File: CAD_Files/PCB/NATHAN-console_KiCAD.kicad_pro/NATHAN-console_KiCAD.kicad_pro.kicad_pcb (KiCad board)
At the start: 2 copper layers, 93 x 84 mm, 38 parts

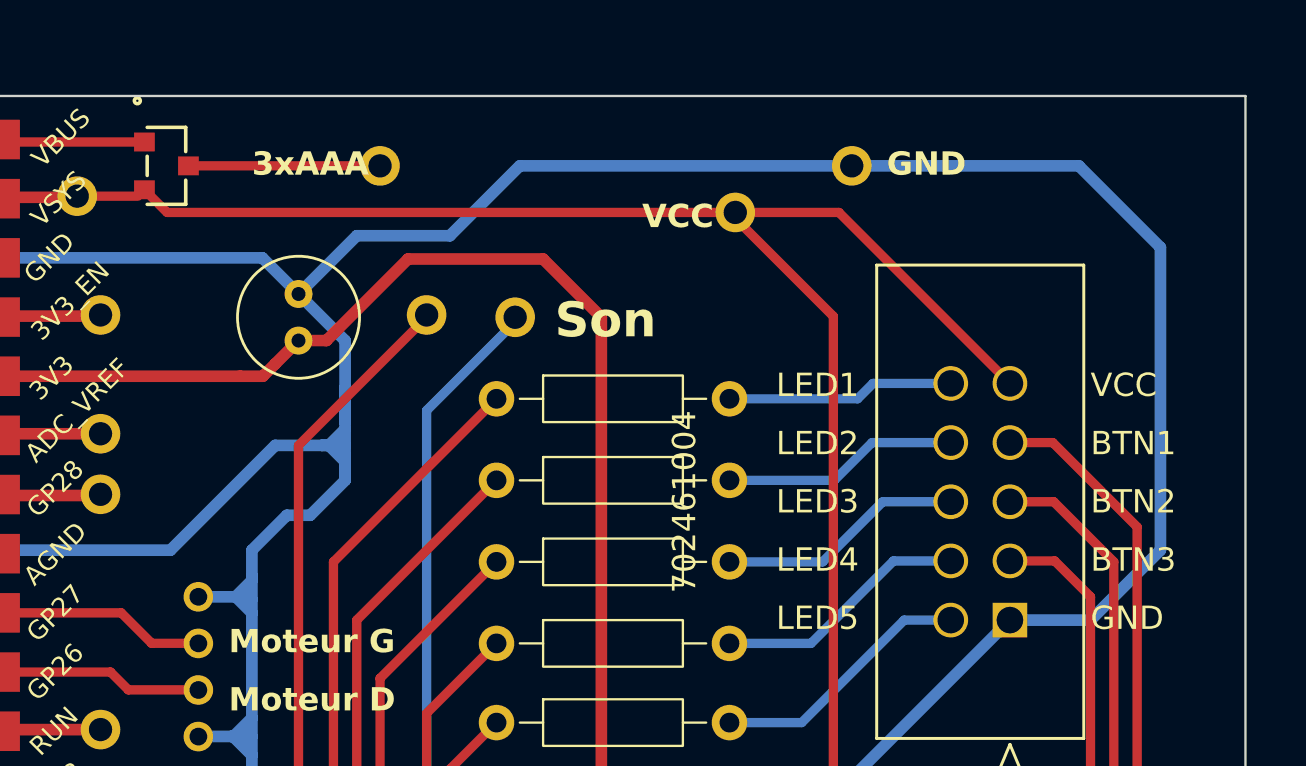
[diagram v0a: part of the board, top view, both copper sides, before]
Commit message: Add footprint information for Reverb modules and create autosave lock file
- Added fp-info-cache for two Reverb modules (BTDR-1H and BTDR-1V) with relevant details and links.
- Created an autosave lock file for the KiCAD project to prevent concurrent edits.
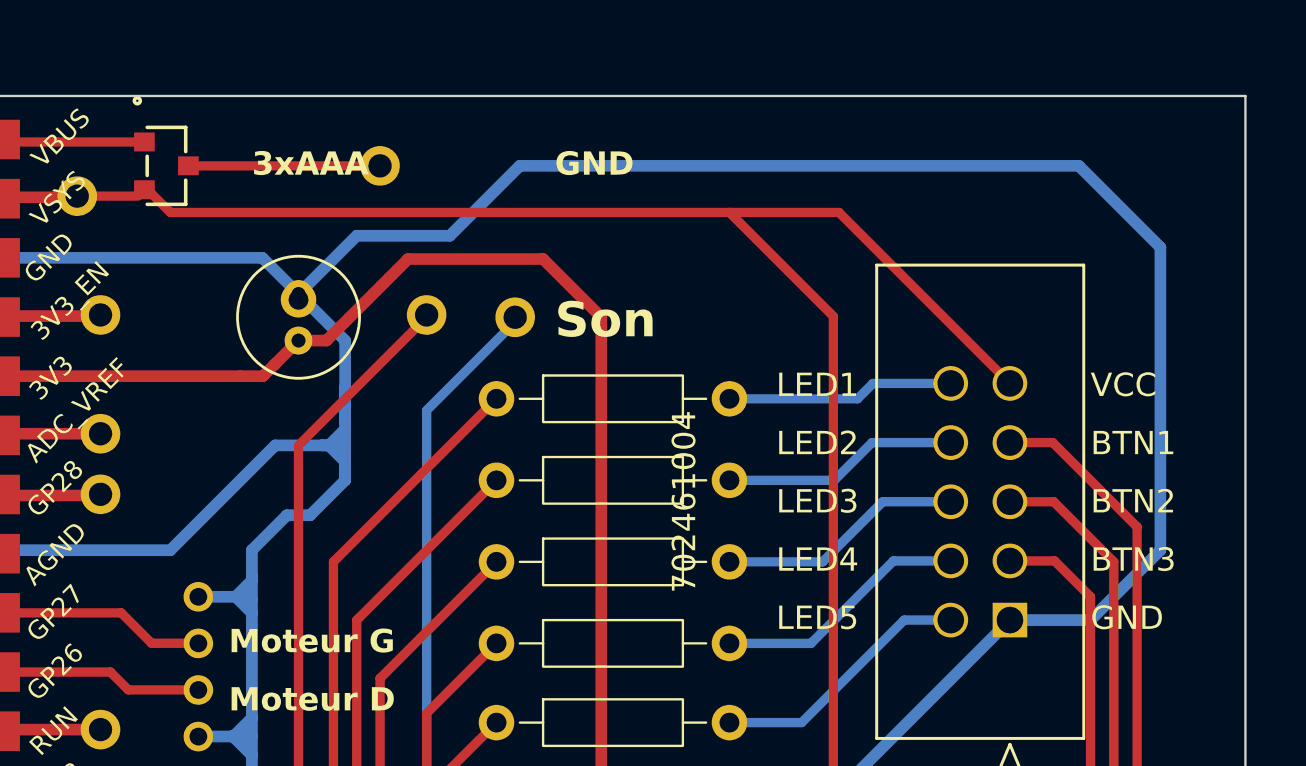
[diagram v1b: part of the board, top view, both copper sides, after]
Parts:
- removed the ? at (374.2, 154.0)
- removed the ? at (379.2, 152.0)
- added ?: , , F.Cu at (374.0, 154.0)
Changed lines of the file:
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@@
 	(footprint ""
 		(layer "F.Cu")
-		(at 309 170)
+		(at 374 154)
 		(property "Reference" ""
 			(at 0 0 0)
@@
 		)
 		(pad "1" thru_hole circle
-			(at 0 0)
-			(size 1.7 1.7)
-			(drill 1)
+			(at -18.5 3.75)
+			(size 1.524 1.524)
+			(drill 0.85)
 			(layers "*.Cu" "*.Mask")
 			(remove_unused_layers no)
+			(net 3 "VCC")
 		)
 	)
 	(footprint ""
 		(layer "F.Cu")
-		(at 315 189)
+		(at 309 170)
 		(property "Reference" ""
 			(at 0 0 0)
@@
 	(footprint ""
 		(layer "F.Cu")
-		(at 379.25 152)
+		(at 315 189)
 		(property "Reference" ""
 			(at 0 0 0)
@@
 			(layers "*.Cu" "*.Mask")
 			(remove_unused_layers no)
-			(net 1 "GND")
 		)
 	)
@@
 	(footprint ""
 		(layer "F.Cu")
-		(at 374.25 154)
-		(property "Reference" ""
-			(at 0 0 0)
-			(unlocked yes)
-			(layer "F.SilkS")
-			(effects
-				(font
-					(size 1.27 1.27)
-				)
-			)
-		)
-		(property "Value" ""
-			(at 0 0 0)
-			(unlocked yes)
-			(layer "F.Fab")
-			(effects
-				(font
-					(size 1.27 1.27)
-				)
-			)
-		)
-		(property "Footprint" ""
-			(at 0 0 0)
-			(unlocked yes)
-			(layer "F.Fab")
-			(hide yes)
-			(effects
-				(font
-					(size 1.27 1.27)
-				)
-			)
-		)
-		(property "Datasheet" ""
-			(at 0 0 0)
-			(unlocked yes)
-			(layer "F.Fab")
-			(hide yes)
-			(effects
-				(font
-					(size 1.27 1.27)
-				)
-			)
-		)
-		(property "Description" ""
-			(at 0 0 0)
-			(unlocked yes)
-			(layer "F.Fab")
-			(hide yes)
-			(effects
-				(font
-					(size 1.27 1.27)
-				)
-			)
-		)
-		(pad "1" thru_hole circle
-			(at 0 0)
-			(size 1.7 1.7)
-			(drill 1)
-			(layers "*.Cu" "*.Mask")
-			(remove_unused_layers no)
-			(net 3 "VCC")
-		)
-	)
-	(footprint ""
-		(layer "F.Cu")
 		(at 359 152)
 		(property "Reference" ""
@@
 		)
 	)
-	(gr_text "VCC"
-		(at 370.25 154.75 0)
-		(layer "F.SilkS")
-		(effects
-			(font
-				(size 1 1)
-				(thickness 0.2)
-				(bold yes)
-			)
-			(justify left bottom)
-		)
-	)
 	(gr_text "Son"
 		(at 366.5 159.5 0)
@@
 	)
 	(gr_text "GND"
-		(at 380.75 152.5 0)
+		(at 366.5 152.5 0)
 		(layer "F.SilkS")
 		(effects
@@
 	)
 	(segment
-		(start 358 155)
-		(end 355.5 157.5)
-		(width 0.5)
-		(layer "B.Cu")
-		(net 1)
-	)
-	(segment
 		(start 352.795101 170.5)
 		(end 352.8 170.495101)
@@
 	)
 	(segment
-		(start 386.04 171.5)
-		(end 389.5 171.5)
-		(width 0.5)
-		(layer "B.Cu")
-		(net 1)
-	)
-	(segment
 		(start 353.5 180.7)
 		(end 353.5 180.6)
@@
 	)
 	(segment
-		(start 379.25 152)
-		(end 365 152)
+		(start 354.5 164)
+		(end 356.5 164)
 		(width 0.5)
 		(layer "B.Cu")
@@
 	)
 	(segment
-		(start 354.5 164)
-		(end 356.5 164)
+		(start 311 180.5)
+		(end 311 180.9)
 		(width 0.5)
 		(layer "B.Cu")
@@
 	)
 	(segment
-		(start 311 180.5)
-		(end 311 180.9)
+		(start 365 152)
+		(end 389 152)
 		(width 0.5)
 		(layer "B.Cu")
@@
 	)
 	(segment
-		(start 365 152)
-		(end 362 155)
-		(width 0.5)
-		(layer "B.Cu")
-		(net 1)
-	)
-	(segment
 		(start 311 181.8)
 		(end 311 181.75)
@@
 	)
 	(segment
+		(start 362 155)
+		(end 358 155)
+		(width 0.5)
+		(layer "B.Cu")
+		(net 1)
+	)
+	(segment
 		(start 352.6 176.495099)
 		(end 353.495099 176.495099)
@@
 	)
 	(segment
-		(start 389 152)
-		(end 379.25 152)
+		(start 357.5 163)
+		(end 357.5 163.3)
 		(width 0.5)
 		(layer "B.Cu")
@@
 	)
 	(segment
-		(start 357.5 163)
-		(end 357.5 163.3)
+		(start 392.5 168.5)
+		(end 389.5 171.5)
 		(width 0.5)
 		(layer "B.Cu")
@@
 	)
 	(segment
+		(start 365 152)
+		(end 362 155)
+		(width 0.5)
+		(layer "B.Cu")
+		(net 1)
+	)
+	(segment
 		(start 313.35 168.65)
 		(end 311.85 168.65)
@@
 	)
 	(segment
+		(start 389.5 171.5)
+		(end 386.04 171.5)
+		(width 0.5)
+		(layer "B.Cu")
+		(net 1)
+	)
+	(segment
 		(start 323.11 181.35)
 		(end 312.1 181.35)
@@
 	)
 	(segment
-		(start 389.5 171.5)
-		(end 392.5 168.5)
-		(width 0.5)
-		(layer "B.Cu")
-		(net 1)
-	)
-	(segment
 		(start 353.95 155.95)
 		(end 355.5 157.5)
@@
 	)
 	(segment
-		(start 392.5 168.5)
+		(start 389 152)
 		(end 392.5 155.5)
 		(width 0.5)
@@
 	)
 	(segment
-		(start 311 176.9)
-		(end 311 180.5)
+		(start 358 155)
+		(end 355.5 157.5)
 		(width 0.5)
 		(layer "B.Cu")
@@
 	)
 	(segment
-		(start 311 175.2)
-		(end 311 175.1)
+		(start 311 176.9)
+		(end 311 180.5)
 		(width 0.5)
 		(layer "B.Cu")
@@
 	)
 	(segment
-		(start 392.5 155.5)
-		(end 389 152)
+		(start 311 175.2)
+		(end 311 175.1)
 		(width 0.5)
 		(layer "B.Cu")
@@
 	)
 	(segment
+		(start 392.5 155.5)
+		(end 392.5 168.5)
+		(width 0.5)
+		(layer "B.Cu")
+		(net 1)
+	)
+	(segment
 		(start 309.5 224)
 		(end 312 226.5)
@@
 	)
 	(segment
-		(start 362 155)
-		(end 358 155)
-		(width 0.5)
-		(layer "B.Cu")
-		(net 1)
-	)
-	(segment
 		(start 312 226.5)
 		(end 316.5 226.5)
@@
 	)
 	(segment
-		(start 378.46 158.46)
-		(end 374.25 154.25)
+		(start 348.885001 153.024999)
+		(end 349.024999 153.024999)
 		(width 0.4)
 		(layer "F.Cu")
@@
 	)
 	(segment
-		(start 386.04 161.34)
-		(end 378.7 154)
-		(width 0.4)
+		(start 340.95 153.35)
+		(end 345.95 153.35)
+		(width 0.5)
 		(layer "F.Cu")
 		(net 3)
 	)
 	(segment
-		(start 340.95 153.35)
-		(end 345.95 153.35)
-		(width 0.5)
+		(start 378.7 154)
+		(end 386.04 161.34)
+		(width 0.4)
 		(layer "F.Cu")
 		(net 3)
@@
 	)
 	(segment
-		(start 349.860002 154)
-		(end 348.885001 153.024999)
-		(width 0.4)
-		(layer "F.Cu")
-		(net 3)
-	)
-	(segment
 		(start 356.7 159.5)
 		(end 360.2 156)
@@
 	)
 	(segment
-		(start 374.25 154.25)
-		(end 374.25 154)
+		(start 374 154)
+		(end 350 154)
 		(width 0.4)
 		(layer "F.Cu")
@@
 	)
 	(segment
-		(start 374.25 154)
-		(end 349.860002 154)
+		(start 378.46 158.46)
+		(end 374 154)
 		(width 0.4)
 		(layer "F.Cu")
@@
 	)
 	(segment
-		(start 355.3 204.4)
-		(end 351.6 204.4)
-		(width 0.5)
-		(layer "F.Cu")
-		(net 3)
-	)
-	(segment
 		(start 378.7 154)
-		(end 374.25 154)
+		(end 374 154)
 		(width 0.4)
 		(layer "F.Cu")
@@
 	)
 	(segment
-		(start 378.46 187)
-		(end 378.46 158.46)
-		(width 0.4)
+		(start 355.3 204.4)
+		(end 351.6 204.4)
+		(width 0.5)
 		(layer "F.Cu")
 		(net 3)
@@
 		(layer "F.Cu")
 		(net 3)
+	)
+	(segment
+		(start 349.024999 153.024999)
+		(end 350 154)
+		(width 0.4)
+		(layer "F.Cu")
+		(net 3)
+	)
+	(segment
+		(start 378.46 187)
+		(end 378.46 158.46)
+		(width 0.4)
+		(layer "F.Cu")
+		(net 3)

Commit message: fix: pcb errors
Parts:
- moved ? 2.50 mm to (375.5, 152.0)
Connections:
- ? pad 1: VCC -> 3V3
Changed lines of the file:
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@@
+	(footprint ""
+		(layer "F.Cu")
+		(at 375.5 152)
+		(property "Reference" ""
+			(at 0 0 0)
+			(unlocked yes)
+			(layer "F.SilkS")
+			(effects
+				(font
+					(size 1.27 1.27)
+				)
+			)
+		)
+		(property "Value" ""
+			(at 0 0 0)
+			(unlocked yes)
+			(layer "F.Fab")
+			(effects
+				(font
+					(size 1.27 1.27)
+				)
+			)
+		)
+		(property "Footprint" ""
+			(at 0 0 0)
+			(unlocked yes)
+			(layer "F.Fab")
+			(hide yes)
+			(effects
+				(font
+					(size 1.27 1.27)
+				)
+			)
+		)
+		(property "Datasheet" ""
+			(at 0 0 0)
+			(unlocked yes)
+			(layer "F.Fab")
+			(hide yes)
+			(effects
+				(font
+					(size 1.27 1.27)
+				)
+			)
+		)
+		(property "Description" ""
+			(at 0 0 0)
+			(unlocked yes)
+			(layer "F.Fab")
+			(hide yes)
+			(effects
+				(font
+					(size 1.27 1.27)
+				)
+			)
+		)
+		(pad "1" thru_hole circle
+			(at 0 0)
+			(size 1.7 1.7)
+			(drill 1)
+			(layers "*.Cu" "*.Mask")
+			(remove_unused_layers no)
+			(net 2 "3V3")
+		)
+	)
 	(footprint ""
 		(layer "F.Cu")
@@
 		)
 	)
-	(footprint ""
-		(layer "F.Cu")
-		(at 374 154)
-		(property "Reference" ""
-			(at 0 0 0)
-			(unlocked yes)
-			(layer "F.SilkS")
-			(effects
-				(font
-					(size 1.27 1.27)
-				)
-			)
-		)
-		(property "Value" ""
-			(at 0 0 0)
-			(unlocked yes)
-			(layer "F.Fab")
-			(effects
-				(font
-					(size 1.27 1.27)
-				)
-			)
-		)
-		(property "Footprint" ""
-			(at 0 0 0)
-			(unlocked yes)
-			(layer "F.Fab")
-			(hide yes)
-			(effects
-				(font
-					(size 1.27 1.27)
-				)
-			)
-		)
-		(property "Datasheet" ""
-			(at 0 0 0)
-			(unlocked yes)
-			(layer "F.Fab")
-			(hide yes)
-			(effects
-				(font
-					(size 1.27 1.27)
-				)
-			)
-		)
-		(property "Description" ""
-			(at 0 0 0)
-			(unlocked yes)
-			(layer "F.Fab")
-			(hide yes)
-			(effects
-				(font
-					(size 1.27 1.27)
-				)
-			)
-		)
-		(pad "1" thru_hole circle
-			(at -18.5 3.75)
-			(size 1.524 1.524)
-			(drill 0.85)
-			(layers "*.Cu" "*.Mask")
-			(remove_unused_layers no)
-			(net 3 "VCC")
-		)
-	)
